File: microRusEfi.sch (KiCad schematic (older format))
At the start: 13 parts, among them U3 Molex_48_pin

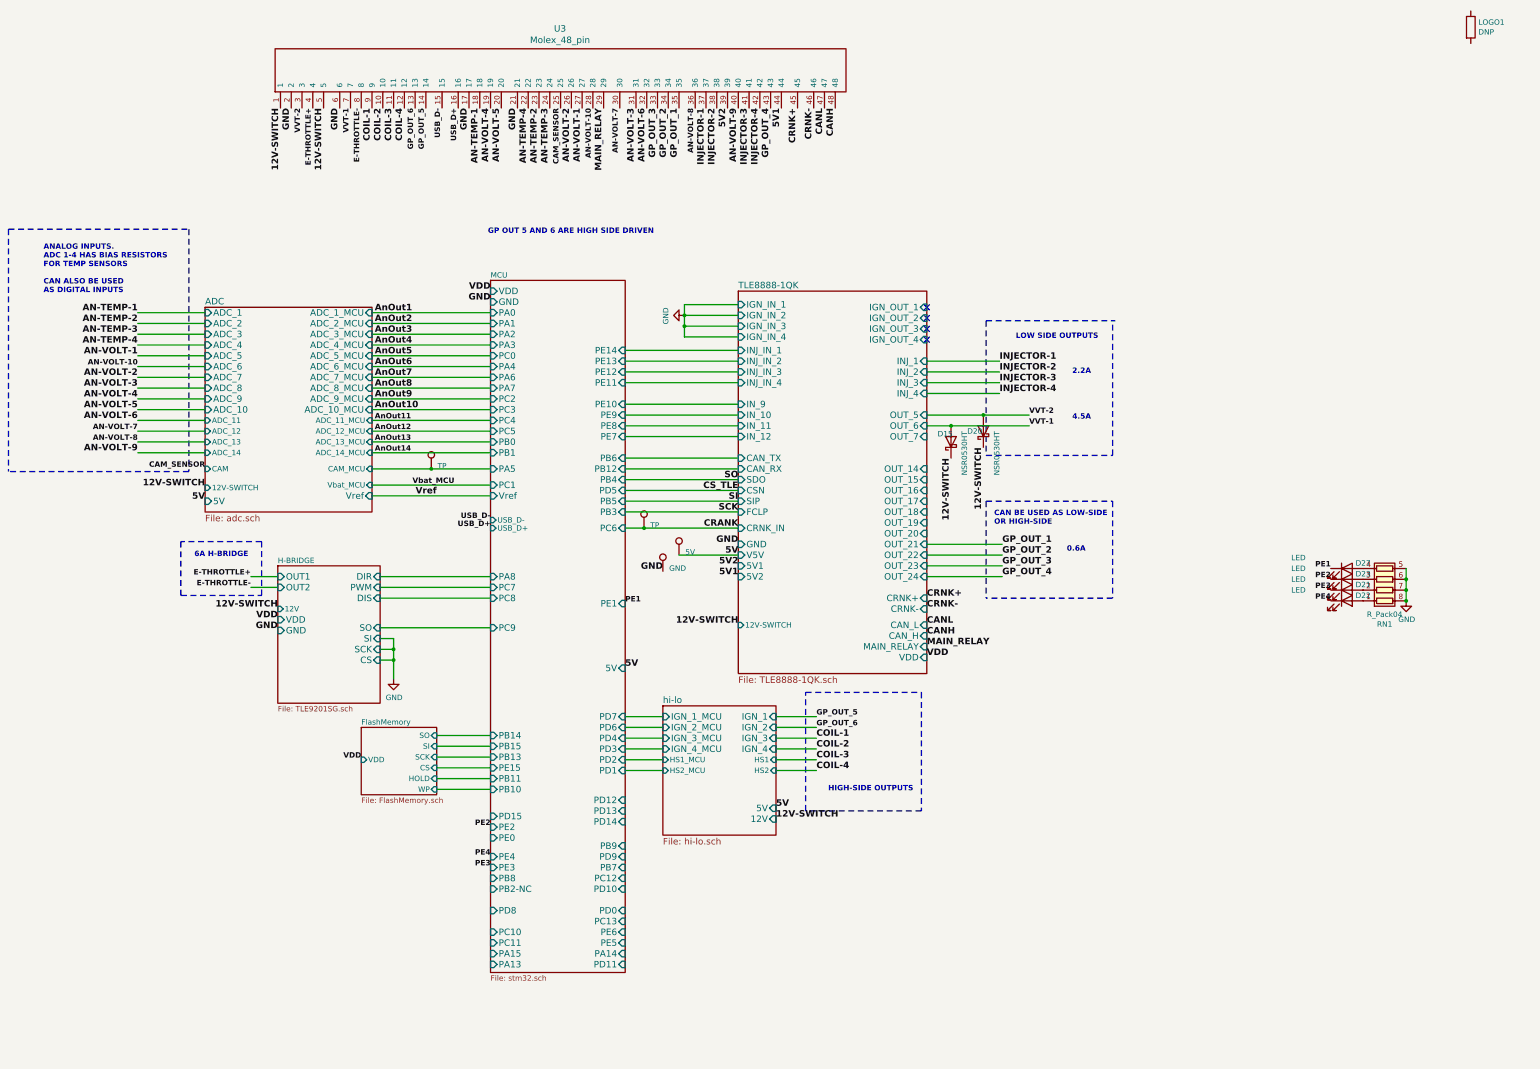
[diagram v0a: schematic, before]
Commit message: from Ola and Jared (#71)
* Update

* removed fp-info-cache from git

* Gerbers

* moved connector

* Mostly Ola's e-mailed copy, plus some of my own fixes to his almost done revision. I also did some house cleaning, with boundary edges, removed most DRC and ERC errors, etc.

* added Fiducial's
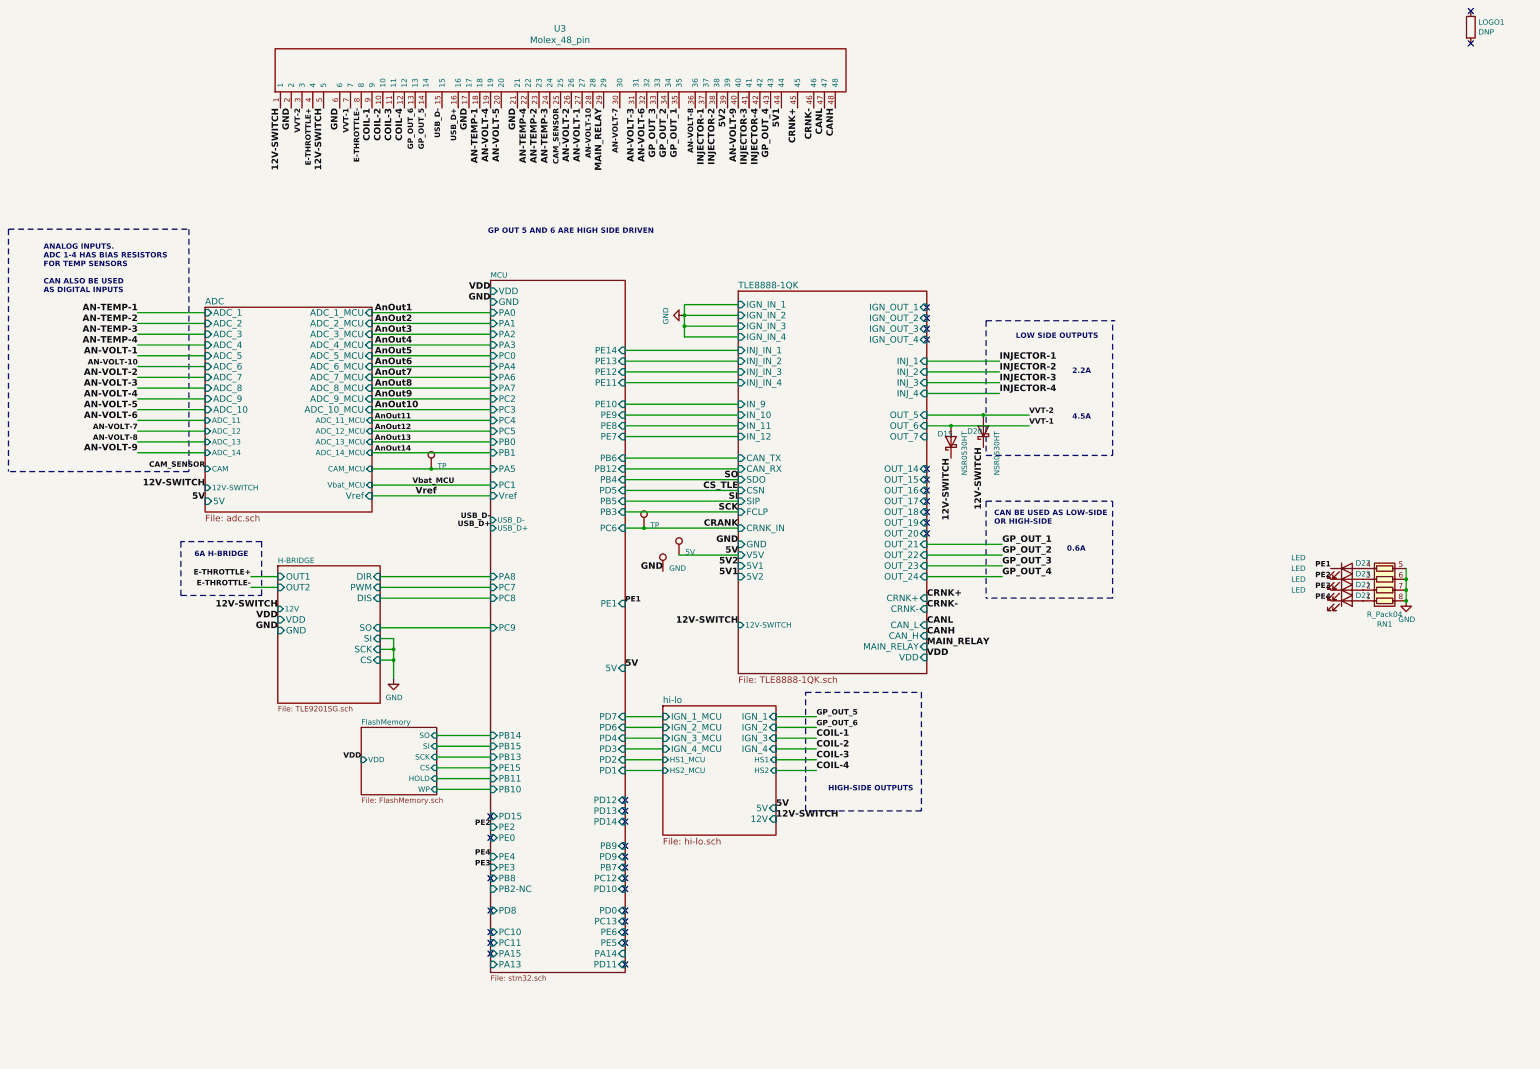
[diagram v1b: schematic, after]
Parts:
- D21, D22, D23, D27: footprint LED_SMD:LED_0402_1005Metric -> LED_SMD:LED_0603_1608Metric
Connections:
- no-connect marks 4 -> 33
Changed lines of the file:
@@
 EELAYER 29 0
 EELAYER END
-$Descr User 17000 12598
+$Descr B 17000 11000
 encoding utf-8
 Sheet 1 7
 Title "microRusEfi"
-Date "2019-01-31"
-Rev "R2.1"
+Date "2019-07-01"
+Rev "R0.2"
 Comp ""
 Comment1 ""
@@
 F 0 "D22" H 14800 6200 50  0000 C CNN
 F 1 "LED" H 14200 6250 50  0000 C CNN
-F 2 "LED_SMD:LED_0402_1005Metric" H 14650 6150 50  0001 C CNN
+F 2 "LED_SMD:LED_0603_1608Metric" H 14650 6150 50  0001 C CNN
 F 3 "~" H 14650 6150 50  0001 C CNN
 	1    14650 6150
@@
 F 0 "D21" H 14800 6100 50  0000 C CNN
 F 1 "LED" H 14200 6150 50  0000 C CNN
-F 2 "LED_SMD:LED_0402_1005Metric" H 14650 6050 50  0001 C CNN
+F 2 "LED_SMD:LED_0603_1608Metric" H 14650 6050 50  0001 C CNN
 F 3 "~" H 14650 6050 50  0001 C CNN
 	1    14650 6050
@@
 F 0 "D23" H 14800 6000 50  0000 C CNN
 F 1 "LED" H 14200 6050 50  0000 C CNN
-F 2 "LED_SMD:LED_0402_1005Metric" H 14650 5950 50  0001 C CNN
+F 2 "LED_SMD:LED_0603_1608Metric" H 14650 5950 50  0001 C CNN
 F 3 "~" H 14650 5950 50  0001 C CNN
 	1    14650 5950
@@
 F 0 "D27" H 14800 5900 50  0000 C CNN
 F 1 "LED" H 14200 5950 50  0000 C CNN
-F 2 "LED_SMD:LED_0402_1005Metric" H 14650 5850 50  0001 C CNN
+F 2 "LED_SMD:LED_0603_1608Metric" H 14650 5850 50  0001 C CNN
 F 3 "~" H 14650 5850 50  0001 C CNN
 	1    14650 5850
@@
 Wire Wire Line
 	15200 6050 15200 6150
+NoConn ~ 7950 8000
+NoConn ~ 7950 8100
+NoConn ~ 7950 8200
+NoConn ~ 7950 8425
+NoConn ~ 7950 8525
+NoConn ~ 7950 8625
+NoConn ~ 7950 8725
+NoConn ~ 7950 9025
+NoConn ~ 7950 9125
+NoConn ~ 7950 9225
+NoConn ~ 7950 9325
+NoConn ~ 7950 9525
+NoConn ~ 6700 9425
+NoConn ~ 6700 9325
+NoConn ~ 6700 9225
+NoConn ~ 6700 9025
+NoConn ~ 10750 5525
+NoConn ~ 10750 5425
+NoConn ~ 10750 5225
+NoConn ~ 10750 5125
+NoConn ~ 10750 5325
+NoConn ~ 10750 5025
+NoConn ~ 10750 4925
+NoConn ~ 15800 675
+NoConn ~ 15800 975
+NoConn ~ 6700 8350
+NoConn ~ 6700 8725
+NoConn ~ 6700 8150
+NoConn ~ 7950 8825
 $EndSCHEMATC

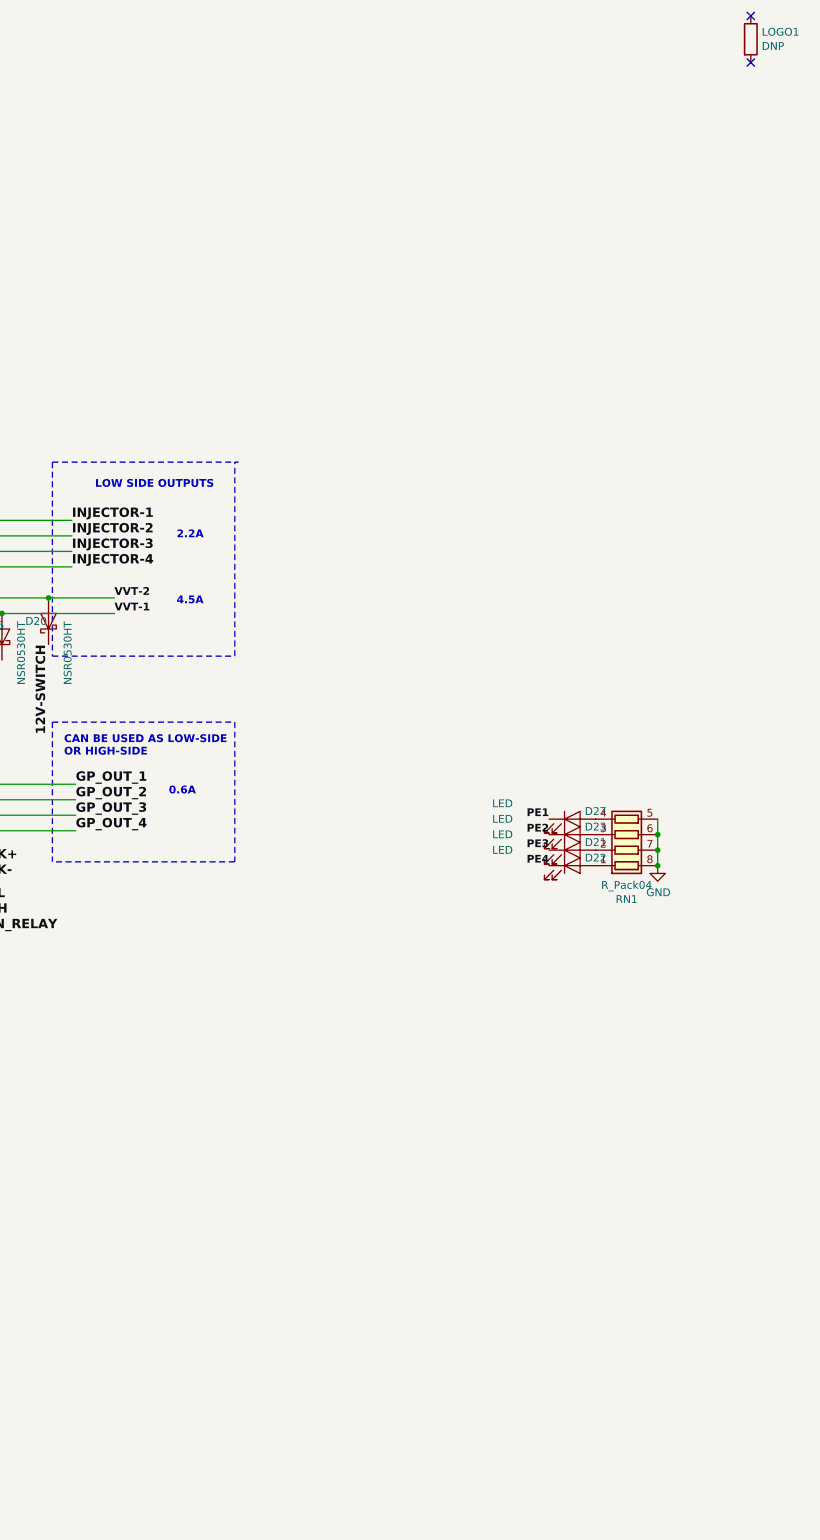
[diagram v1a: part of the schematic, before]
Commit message: Updated logo symbol and footprint, BOM is 99% entered in KC schematic now.
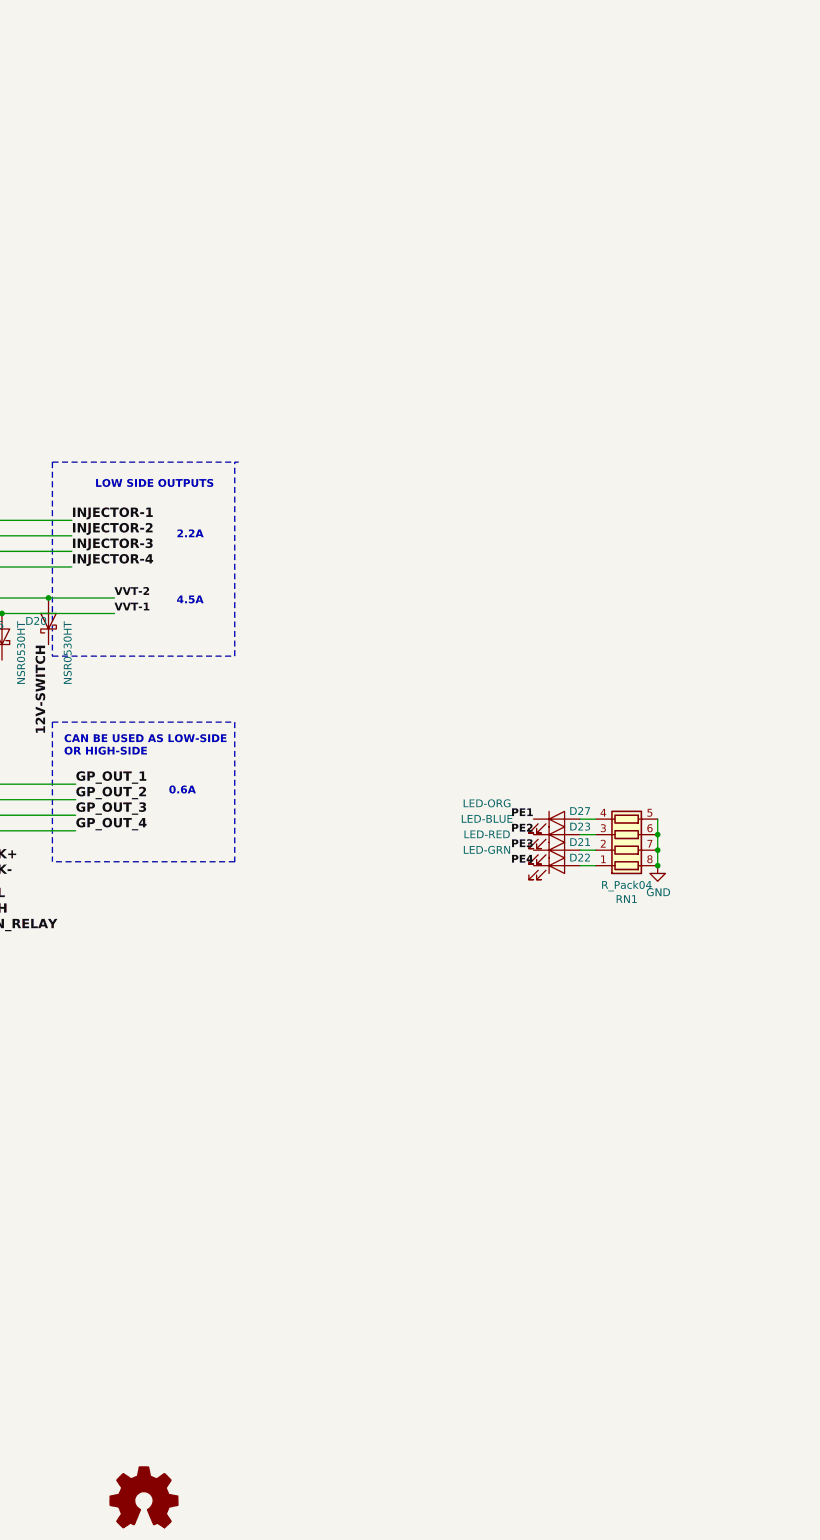
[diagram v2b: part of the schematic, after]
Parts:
- removed LOGO1: DNP, modules:Logo, symbol Device:R
- added LOGO1: DNP, modules:Logo, symbol Graphic:Logo_Open_Hardware_Small
- D15, D20: Manufacturer (none) -> ON-SEMI; VEND (none) -> DIGI; VEND# (none) -> NSR0530HT1GOSCT-ND
- D21: value LED -> LED-RED; Manufacturer (none) -> Lite-On; Part # (none) -> LTST-S270KRKT; VEND (none) -> DIGI; VEND# (none) -> 160-1479-1-ND
- D22: value LED -> LED-GRN; Manufacturer (none) -> Lite-On; Part # (none) -> LTST-C191KGKT; VEND (none) -> DIGI; VEND# (none) -> 160-1446-1-ND
- D23: value LED -> LED-BLUE; Manufacturer (none) -> Lite-On; Part # (none) -> LTST-C193TBKT-5A; VEND (none) -> DIGI; VEND# (none) -> 160-1827-1-ND
- D27: value LED -> LED-ORG; Manufacturer (none) -> Lite-On; Part # (none) -> LTST-C190KFKT; VEND (none) -> DIGI; VEND# (none) -> 160-1434-1-ND
- RN1: Manufacturer (none) -> mm; Part # (none) -> dd; VEND (none) -> DIGI; VEND# (none) -> vv
- TP1, TP2, TP3, TP4: Manufacturer (none) -> DNP; Part # (none) -> DNP; VEND (none) -> DNP; VEND# (none) -> DNP
- U3: VEND (none) -> DIGI; VEND# (none) -> WM4430-ND
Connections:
- no-connect marks 33 -> 31
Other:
- moved on the sheet: D21, D22, D23, D27
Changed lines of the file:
@@
 F 2 "TestPoint:TestPoint_Pad_D4.0mm" H 8650 5725 50  0001 C CNN
 F 3 "~" H 8650 5725 50  0001 C CNN
+F 4 "DNP" H 0   0   50  0001 C CNN "Part #"
+F 5 "DNP" H 0   0   50  0001 C CNN "VEND"
+F 6 "DNP" H 0   0   50  0001 C CNN "VEND#"
+F 7 "DNP" H 0   0   50  0001 C CNN "Manufacturer"
 	1    8450 5725
 	1    0    0    -1
@@
 F 4 "MOLEX" H 0   0   50  0001 C CNN "Manufacturer"
 F 5 "500762-0481" H 0   0   50  0001 C CNN "Part #"
+F 6 "DIGI" H 0   0   50  0001 C CNN "VEND"
+F 7 "WM4430-ND" H 0   0   50  0001 C CNN "VEND#"
 	1    7750 2125
 	0    -1   -1   0
@@
 F 3 "~" H 10975 4675 50  0001 C CNN
 F 4 "NSR0530HT" H 0   0   50  0001 C CNN "Part #"
+F 5 "DIGI" H 0   0   50  0001 C CNN "VEND"
+F 6 "NSR0530HT1GOSCT-ND" H 0   0   50  0001 C CNN "VEND#"
+F 7 "ON-SEMI" H 0   0   50  0001 C CNN "Manufacturer"
 	1    10975 4675
 	0    -1   -1   0
@@
 F 3 "~" H 11275 4575 50  0001 C CNN
 F 4 "NSR0530HT" H 0   0   50  0001 C CNN "Part #"
+F 5 "DIGI" H 0   0   50  0001 C CNN "VEND"
+F 6 "NSR0530HT1GOSCT-ND" H 0   0   50  0001 C CNN "VEND#"
+F 7 "ON-SEMI" H 0   0   50  0001 C CNN "Manufacturer"
 	1    11275 4575
 	0    -1   -1   0
@@
 F 2 "TestPoint:TestPoint_Pad_D4.0mm" H 8500 5875 50  0001 C CNN
 F 3 "~" H 8500 5875 50  0001 C CNN
+F 4 "DNP" H 0   0   50  0001 C CNN "Part #"
+F 5 "DNP" H 0   0   50  0001 C CNN "Manufacturer"
+F 6 "DNP" H 0   0   50  0001 C CNN "VEND"
+F 7 "DNP" H 0   0   50  0001 C CNN "VEND#"
 	1    8300 5875
 	1    0    0    -1
@@
 Text Label 11275 4725 3    60   ~ 12
 12V-SWITCH
-$Comp
-L Device:R LOGO1
-U 1 1 5D002597
-P 15800 825
-F 0 "LOGO1" H 15870 871 50  0000 L CNN
-F 1 "DNP" H 15870 780 50  0000 L CNN
-F 2 "modules:Logo" V 15730 825 50  0001 C CNN
-F 3 "~" H 15800 825 50  0001 C CNN
-	1    15800 825
-	1    0    0    -1
-$EndComp
 Text Label 7450 1575 3    60   ~ 12
 AN-VOLT-2
@@
 Text Label 6700 8525 2    50   ~ 10
 PE4
-Text Label 14500 5850 2    50   ~ 10
+Text Label 14400 5850 2    50   ~ 10
 PE1
 $Comp
 L Device:LED D22
 U 1 1 5E7651E5
-P 14650 6150
-F 0 "D22" H 14800 6200 50  0000 C CNN
-F 1 "LED" H 14200 6250 50  0000 C CNN
-F 2 "LED_SMD:LED_0603_1608Metric" H 14650 6150 50  0001 C CNN
-F 3 "~" H 14650 6150 50  0001 C CNN
-	1    14650 6150
+P 14550 6150
+F 0 "D22" H 14700 6200 50  0000 C CNN
+F 1 "LED-GRN" H 14100 6250 50  0000 C CNN
+F 2 "LED_SMD:LED_0603_1608Metric" H 14550 6150 50  0001 C CNN
+F 3 "~" H 14550 6150 50  0001 C CNN
+F 4 "LTST-C191KGKT" H -100 0   50  0001 C CNN "Part #"
+F 5 "DIGI" H -100 0   50  0001 C CNN "VEND"
+F 6 "160-1446-1-ND" H -100 0   50  0001 C CNN "VEND#"
+F 7 "Lite-On " H -100 0   50  0001 C CNN "Manufacturer"
+	1    14550 6150
 	1    0    0    -1
 $EndComp
@@
 F 2 "TestPoint:TestPoint_Pad_D2.0mm" H 8325 5475 50  0001 C CNN
 F 3 "~" H 8325 5475 50  0001 C CNN
+F 4 "DNP" H 0   0   50  0001 C CNN "Part #"
+F 5 "DNP" H 0   0   50  0001 C CNN "VEND"
+F 6 "DNP" H 0   0   50  0001 C CNN "VEND#"
+F 7 "DNP" H 0   0   50  0001 C CNN "Manufacturer"
 	1    8125 5475
 	1    0    0    -1
@@
 F 2 "TestPoint:TestPoint_Pad_D2.0mm" H 6350 4925 50  0001 C CNN
 F 3 "~" H 6350 4925 50  0001 C CNN
+F 4 "DNP" H 0   0   50  0001 C CNN "Part #"
+F 5 "DNP" H 0   0   50  0001 C CNN "VEND"
+F 6 "DNP" H 0   0   50  0001 C CNN "VEND#"
+F 7 "DNP" H 0   0   50  0001 C CNN "Manufacturer"
 	1    6150 4925
 	1    0    0    -1
@@
 L Device:LED D21
 U 1 1 5D1B59E8
-P 14650 6050
-F 0 "D21" H 14800 6100 50  0000 C CNN
-F 1 "LED" H 14200 6150 50  0000 C CNN
-F 2 "LED_SMD:LED_0603_1608Metric" H 14650 6050 50  0001 C CNN
-F 3 "~" H 14650 6050 50  0001 C CNN
-	1    14650 6050
+P 14550 6050
+F 0 "D21" H 14700 6100 50  0000 C CNN
+F 1 "LED-RED" H 14100 6150 50  0000 C CNN
+F 2 "LED_SMD:LED_0603_1608Metric" H 14550 6050 50  0001 C CNN
+F 3 "~" H 14550 6050 50  0001 C CNN
+F 4 "LTST-S270KRKT" H -100 0   50  0001 C CNN "Part #"
+F 5 "DIGI" H -100 0   50  0001 C CNN "VEND"
+F 6 "160-1479-1-ND" H -100 0   50  0001 C CNN "VEND#"
+F 7 "Lite-On " H -100 0   50  0001 C CNN "Manufacturer"
+	1    14550 6050
 	1    0    0    -1
 $EndComp
@@
 L Device:LED D23
 U 1 1 5D1BAEB2
-P 14650 5950
-F 0 "D23" H 14800 6000 50  0000 C CNN
-F 1 "LED" H 14200 6050 50  0000 C CNN
-F 2 "LED_SMD:LED_0603_1608Metric" H 14650 5950 50  0001 C CNN
-F 3 "~" H 14650 5950 50  0001 C CNN
-	1    14650 5950
+P 14550 5950
+F 0 "D23" H 14700 6000 50  0000 C CNN
+F 1 "LED-BLUE" H 14100 6050 50  0000 C CNN
+F 2 "LED_SMD:LED_0603_1608Metric" H 14550 5950 50  0001 C CNN
+F 3 "~" H 14550 5950 50  0001 C CNN
+F 4 "LTST-C193TBKT-5A" H -100 0   50  0001 C CNN "Part #"
+F 5 "DIGI" H -100 0   50  0001 C CNN "VEND"
+F 6 "160-1827-1-ND" H -100 0   50  0001 C CNN "VEND#"
+F 7 "Lite-On " H -100 0   50  0001 C CNN "Manufacturer"
+	1    14550 5950
 	1    0    0    -1
 $EndComp
@@
 L Device:LED D27
 U 1 1 5D1C01C9
-P 14650 5850
-F 0 "D27" H 14800 5900 50  0000 C CNN
-F 1 "LED" H 14200 5950 50  0000 C CNN
-F 2 "LED_SMD:LED_0603_1608Metric" H 14650 5850 50  0001 C CNN
-F 3 "~" H 14650 5850 50  0001 C CNN
-	1    14650 5850
-	1    0    0    -1
-$EndComp
-Text Label 14500 5950 2    50   ~ 10
+P 14550 5850
+F 0 "D27" H 14700 5900 50  0000 C CNN
+F 1 "LED-ORG" H 14100 5950 50  0000 C CNN
+F 2 "LED_SMD:LED_0603_1608Metric" H 14550 5850 50  0001 C CNN
+F 3 "~" H 14550 5850 50  0001 C CNN
+F 4 "LTST-C190KFKT" H -100 0   50  0001 C CNN "Part #"
+F 5 "DIGI" H -100 0   50  0001 C CNN "VEND"
+F 6 "160-1434-1-ND" H -100 0   50  0001 C CNN "VEND#"
+F 7 "Lite-On " H -100 0   50  0001 C CNN "Manufacturer"
+	1    14550 5850
+	1    0    0    -1
+$EndComp
+Text Label 14400 5950 2    50   ~ 10
 PE2
-Text Label 14500 6050 2    50   ~ 10
+Text Label 14400 6050 2    50   ~ 10
 PE3
-Text Label 14500 6150 2    50   ~ 10
+Text Label 14400 6150 2    50   ~ 10
 PE4
 $Comp
@@
 F 2 "Resistor_SMD:R_Array_Convex_4x0603" V 15275 5950 50  0001 C CNN
 F 3 "~" H 15000 5950 50  0001 C CNN
+F 4 "dd" H 0   0   50  0001 C CNN "Part #"
+F 5 "DIGI" H 0   0   50  0001 C CNN "VEND"
+F 6 "vv" H 0   0   50  0001 C CNN "VEND#"
+F 7 "mm" H 0   0   50  0001 C CNN "Manufacturer"
 	1    15000 5950
 	0    1    -1   0
@@
 NoConn ~ 10750 5025
 NoConn ~ 10750 4925
-NoConn ~ 15800 675
-NoConn ~ 15800 975
 NoConn ~ 6700 8350
 NoConn ~ 6700 8725
 NoConn ~ 6700 8150
 NoConn ~ 7950 8825
+$Comp
+L Graphic:Logo_Open_Hardware_Small LOGO1
+U 1 1 5D21BC70
+P 11890 10245
+F 0 "LOGO1" H 11890 10520 50  0001 C CNN
+F 1 "DNP" H 11890 10020 50  0001 C CNN
+F 2 "modules:Logo" H 11890 10245 50  0001 C CNN
+F 3 "~" H 11890 10245 50  0001 C CNN
+F 4 "DNP" H 0   0   50  0001 C CNN "Part #"
+F 5 "DNP" H 0   0   50  0001 C CNN "VEND"
+F 6 "DNP" H 0   0   50  0001 C CNN "VEND#"
+F 7 "DNP" H 0   0   50  0001 C CNN "Manufacturer"
+	1    11890 10245
+	1    0    0    -1
+$EndComp
+Wire Wire Line
+	14700 5850 14800 5850
+Wire Wire Line
+	14700 5950 14800 5950
+Wire Wire Line
+	14700 6050 14800 6050
+Wire Wire Line
+	14700 6150 14800 6150
 $EndSCHEMATC
